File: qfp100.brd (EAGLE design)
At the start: 55.9 x 55.9 mm, 15 parts, among them IC1 F66XX---PZ100EXTENDED

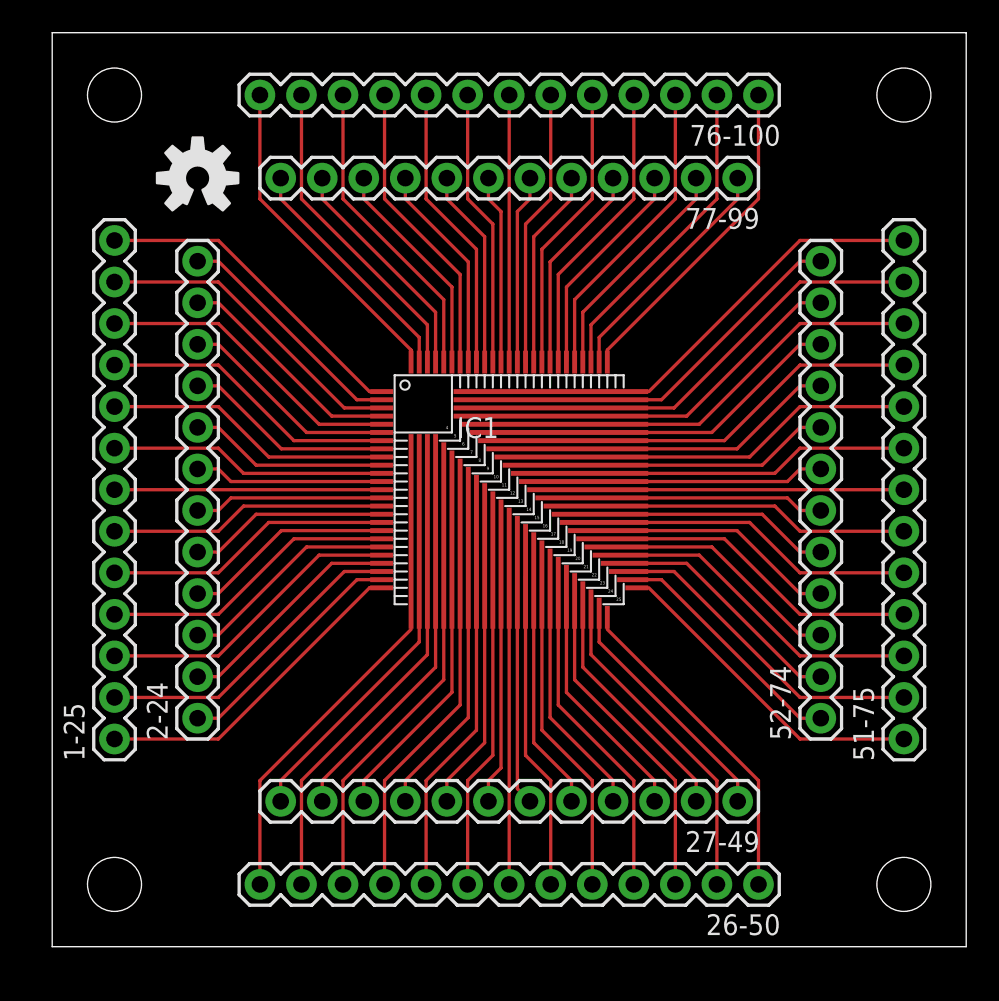
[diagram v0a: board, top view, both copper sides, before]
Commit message: Shrunk board to fit within the 5cmx5cm form factor that allows for very cheap manufacture from services like Seeed Fusion
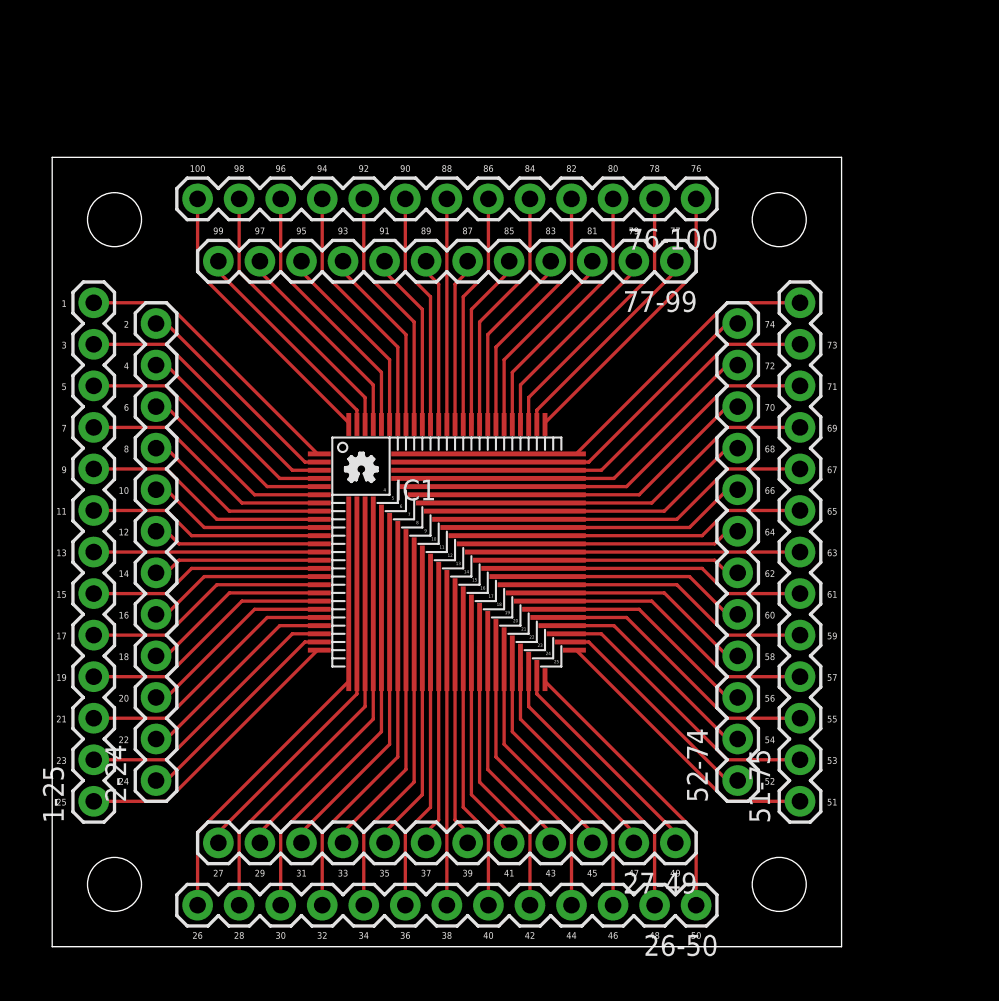
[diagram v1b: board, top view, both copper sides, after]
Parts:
- removed JP5, JP6, JP8: STAND-OFF, SparkFun:STAND-OFF
- added JP1, JP3, JP4: STAND-OFF, SparkFun:STAND-OFF
- U$1: device SparkFun-Aesthetics:OSHW-LOGO-M -> SparkFun-Aesthetics:OSHW-LOGO-XS
- moved U$1 20.4 mm to (18.9, 29.2)
- moved 76-100 7.41 mm to (39.4, 45.7)
- moved 51-75 7.41 mm to (45.7, 8.89)
- moved 52-74 6.35 mm to (41.9, 10.2)
- moved 77-99 6.35 mm to (38.1, 41.9)
- moved IC1 5.39 mm to (24.1, 24.1)
- moved 2-24 4.58 mm to (6.35, 10.2)
- moved 27-49 4.58 mm to (38.1, 6.35)
- moved 26-50 4.02 mm to (39.4, 2.54)
- moved 1-25 4.02 mm to (2.54, 8.89)
- renumbered JP7 to JP2
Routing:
- net 75: track 25.4 -> 22.9 mm
- net 73: track 24.8 -> 22.2 mm
- net 69: track 22.7 -> 20.2 mm
- net 50: track 20.2 -> 17.6 mm
- net 48: track 20.0 -> 17.5 mm
- net 34: track 21.6 -> 19.1 mm
- net 32: track 22.7 -> 20.2 mm
- net 3: track 19.5 -> 17.0 mm
- net 28: track 24.8 -> 22.2 mm
- net 26: track 25.4 -> 22.9 mm
- net 25: track 20.2 -> 17.6 mm
- net 23: track 19.5 -> 17.0 mm
- net 17: track 17.6 -> 15.1 mm
- net 1: track 20.2 -> 17.6 mm
- net 19: track 18.2 -> 15.7 mm
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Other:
- board size 55.9 x 55.9 mm -> 48.3 x 48.3 mm
